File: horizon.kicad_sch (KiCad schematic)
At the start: 102 parts, among them IC1 A3909, J1 Micro_SD_Card_Det1, J10 Conn_01x02_Pin, J2 Conn_02x03_Counter_Clockwise, J7 Conn_02x03_Counter_Clockwise, J8 Conn_02x03_Counter_Clockwise, J9 USB_C_Receptacle_USB2.0_16P, Q2 DMG2301L, SW1 SW_Rotary_1x3_MP, SW2 SW_Rotary_1x3_MP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

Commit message: INTCOMM Completed
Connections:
- net scl: no longer U3.43 (PA22), U4.43 (PA22)
- net sda: no longer U3.44 (PA23), U4.44 (PA23)
- net PTA12: now reaches U1.29 (D4/CAN-RX/PWM)
- net I2C0_SCL: now reaches U1.37 (D19/A5/SCL0/TOUCH)
- net I2C0_SCL: now also U3.44 (PA23), U4.44 (PA23)
- net I2C0_SDA: now reaches U1.38 (D18/A4/SDA0/TOUCH)
- net I2C0_SDA: now also U3.43 (PA22), U4.43 (PA22)
- net PTD4: now reaches U1.57 (D2)
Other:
- note added: "INT from NAV"
- note added: "INT from TLM"
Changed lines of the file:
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@@
 		)
 	)
+	(text "INT from TLM"
+		(exclude_from_sim no)
+		(at 307.086 140.208 0)
+		(effects
+			(font
+				(size 1.27 1.27)
+			)
+		)
+	)
 	(text "GPS → MCU RX"
 		(exclude_from_sim no)
@@
 		)
 	)
-	(text "For NAND and SD"
+	(text "INT from NAV"
 		(exclude_from_sim no)
-		(at 293.37 160.274 0)
+		(at 307.848 135.128 0)
 		(effects
 			(font
@@
 		)
 	)
+	(global_label "PTD4"
+		(shape input)
+		(at 322.58 134.62 180)
+		(fields_autoplaced yes)
+		(effects
+			(font
+				(size 1.27 1.27)
+			)
+			(justify right)
+		)
+		(property "Intersheetrefs" "${INTERSHEET_REFS}"
+			(at 314.8777 134.62 0)
+			(effects
+				(font
+					(size 1.27 1.27)
+				)
+				(justify right)
+				(hide yes)
+			)
+		)
+	)
 	(global_label "SWCLK MMCU"
 		(shape input)
@@
 		)
 	)
-	(global_label "scl"
+	(global_label "I2C0_SDA"
 		(shape input)
 		(at 113.03 198.12 180)
@@
 		)
 		(property "Intersheetrefs" "${INTERSHEET_REFS}"
-			(at 107.2629 198.12 0)
+			(at 101.2153 198.12 0)
 			(effects
 				(font
@@
 		)
 	)
-	(global_label "sda"
+	(global_label "I2C0_SCL"
 		(shape input)
 		(at 113.03 200.66 180)
@@
 		)
 		(property "Intersheetrefs" "${INTERSHEET_REFS}"
-			(at 106.7187 200.66 0)
+			(at 101.2758 200.66 0)
 			(effects
 				(font
@@
 		)
 	)
+	(global_label "I2C0_SCL"
+		(shape input)
+		(at 322.58 177.8 180)
+		(fields_autoplaced yes)
+		(effects
+			(font
+				(size 1.27 1.27)
+			)
+			(justify right)
+		)
+		(property "Intersheetrefs" "${INTERSHEET_REFS}"
+			(at 310.8258 177.8 0)
+			(effects
+				(font
+					(size 1.27 1.27)
+				)
+				(justify right)
+				(hide yes)
+			)
+		)
+	)
 	(global_label "SPI_CLOCK TMCU"
 		(shape input)
@@
 		)
 	)
+	(global_label "PTA12"
+		(shape input)
+		(at 322.58 139.7 180)
+		(fields_autoplaced yes)
+		(effects
+			(font
+				(size 1.27 1.27)
+			)
+			(justify right)
+		)
+		(property "Intersheetrefs" "${INTERSHEET_REFS}"
+			(at 313.8496 139.7 0)
+			(effects
+				(font
+					(size 1.27 1.27)
+				)
+				(justify right)
+				(hide yes)
+			)
+		)
+	)
 	(global_label " SPI0_SCK MMCU"
 		(shape input)
@@
 		)
 	)
-	(global_label "scl"
+	(global_label "I2C0_SDA"
 		(shape input)
 		(at 17.78 194.31 180)
@@
 		)
 		(property "Intersheetrefs" "${INTERSHEET_REFS}"
-			(at 12.0129 194.31 0)
+			(at 5.9653 194.31 0)
 			(effects
 				(font
@@
 		)
 	)
+	(global_label "I2C0_SDA"
+		(shape input)
+		(at 322.58 175.26 180)
+		(fields_autoplaced yes)
+		(effects
+			(font
+				(size 1.27 1.27)
+			)
+			(justify right)
+		)
+		(property "Intersheetrefs" "${INTERSHEET_REFS}"
+			(at 310.7653 175.26 0)
+			(effects
+				(font
+					(size 1.27 1.27)
+				)
+				(justify right)
+				(hide yes)
+			)
+		)
+	)
 	(global_label "bat"
 		(shape input)
@@
 		)
 	)
-	(global_label "sda"
+	(global_label "I2C0_SCL"
 		(shape input)
 		(at 17.78 196.85 180)
@@
 		)
 		(property "Intersheetrefs" "${INTERSHEET_REFS}"
-			(at 11.4687 196.85 0)
+			(at 6.0258 196.85 0)
 			(effects
 				(font

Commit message: Labels
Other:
- note added: "SERCOM Stuff For Firmware INTCOMM"
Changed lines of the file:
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@@
 	(generator_version "9.0")
 	(paper "A4")
+	(text "SERCOM Stuff For Firmware INTCOMM"
+		(exclude_from_sim no)
+		(at 292.608 176.784 0)
+		(effects
+			(font
+				(size 1.27 1.27)
+			)
+		)
+	)
 	(text "For NAND and SD"
 		(exclude_from_sim no)
@@
 		)
 	)
+	(text "SERCOM Stuff For Firmware INTCOMM"
+		(exclude_from_sim no)
+		(at 83.058 199.898 0)
+		(effects
+			(font
+				(size 1.27 1.27)
+			)
+		)
+	)
 	(text "MCU → GPS TX"
 		(exclude_from_sim no)
@@
 		(effects
 			(font
+				(size 1.27 1.27)
+			)
+		)
+	)
+	(text "SERCOM Stuff For Firmware INTCOMM"
+		(exclude_from_sim no)
+		(at -13.462 195.58 0)
+		(effects
+			(font

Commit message: set up hierarchy
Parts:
- removed C10: 4n7, Capacitor_SMD:C_0603_1608Metric, symbol Device:C
- removed C14: 0.1µF, symbol Device:C
- removed C15: 0.1 µF, symbol Device:C
- removed C26: 100n, Capacitor_SMD:C_0603_1608Metric, symbol Device:C
- removed C28, C32, C40, C41, C42, C43: 10uF, Capacitor_SMD:C_0603_1608Metric, symbol Device:C
- removed C29, C37: 10u, Capacitor_SMD:C_0603_1608Metric, symbol Device:C
- removed C30, C38: 2u2, Capacitor_SMD:C_0603_1608Metric, symbol Device:C
- removed C31, C39: 100u, Capacitor_THT:CP_Radial_D4.0mm_P2.00mm, symbol Device:C_Polarized_US
- removed C33: 3.3 nF, Capacitor_SMD:C_0603_1608Metric, symbol Device:C
- removed C34: 22uF, Capacitor_SMD:C_0603_1608Metric, symbol Device:C
- removed C35: 1uF, Capacitor_SMD:C_0603_1608Metric, symbol Device:C
- removed C36: 1u, Capacitor_SMD:C_0603_1608Metric, symbol Device:C
- removed D19, D20, D23, D24, D25: PMEG6020ER, Diode_SMD:Nexperia_CFP3_SOD-123W, symbol Diode:PMEG6020ER
- removed D21, D22, D5: LED, LED_SMD:LED_0201_0603Metric, symbol Device:LED
- removed D6: PRTR5V0U2X, Package_TO_SOT_SMD:SOT-143, symbol Power_Protection:PRTR5V0U2X
- removed FL3, FL4: Choke_CommonMode_PulseElectronics_PH9455x105NL, Inductor_THT:L_CommonMode_PulseElectronics_PH9455x105NL_1, symbol Filter:Choke_CommonMode_PulseElectronics_PH9455x105NL
- removed IC1: A3909, A3909:MSOP10-PAD, symbol A3909:A3909
- removed J1: Micro_SD_Card_Det1, symbol Connector:Micro_SD_Card_Det1
- removed J10: Conn_01x02_Pin, Connector_JST:JST_PH_B2B-PH-K_1x02_P2.00mm_Vertical, symbol Connector:Conn_01x02_Pin
- removed J9: USB_C_Receptacle_USB2.0_16P, Connector_USB:USB_C_Receptacle_Amphenol_124019772112A, symbol Connector:USB_C_Receptacle_USB2.0_16P
- removed L2, L3, L4: SLF7055T-6R8N2R8-3PF, Inductor_SMD:L_7.3x7.3_H4.5, symbol SLF7055T-6R8N2R8-3PF[1]:SLF7055T-6R8N2R8-3PF
- removed Q2: DMG2301L, Package_TO_SOT_SMD:SOT-23, symbol Transistor_FET:DMG2301L
- removed R1: 90k, symbol Device:R
- removed R10, R11, R12, R13, R8, R9: 10kΩ, symbol Device:R
- removed R17, R18: 5k1, Resistor_SMD:R_0603_1608Metric, symbol Device:R
- removed R19, R47: 330, Resistor_SMD:R_0603_1608Metric, symbol Device:R
- removed R2: 10k, symbol Device:R
- removed R40, R41, R43, R45, R48, R49, R51: 100k, Resistor_SMD:R_0603_1608Metric, symbol Device:R
- removed R42, R50: 315k, Resistor_SMD:R_0603_1608Metric, symbol Device:R
- removed R44: 350k, Resistor_SMD:R_0603_1608Metric, symbol Device:R
- removed R46: 100, Resistor_SMD:R_0603_1608Metric, symbol Device:R
- removed SW1, SW2: SW_Rotary_1x3_MP, symbol Switch:SW_Rotary_1x3_MP
- removed TP10, TP11: TestPoint, TestPoint:TestPoint_Pad_1.0x1.0mm, symbol Connector:TestPoint
- removed U12: TPS63061, Package_SON:Texas_S-PWSON-N10_ThermalVias, symbol Regulator_Switching:TPS63061
- removed U13: LTC4412xS6, Package_TO_SOT_SMD:TSOT-23-6, symbol Power_Management:LTC4412xS6
- removed U14, U16: TPS61092, Package_DFN_QFN:Texas_RSA_VQFN-16-1EP_4x4mm_P0.65mm_EP2.7x2.7mm_ThermalVias, symbol Regulator_Switching:TPS61092
- removed U15: AP2112K-3.3, Package_TO_SOT_SMD:SOT-23-5, symbol Regulator_Linear:AP2112K-3.3
- removed U2: IMU, BNO086:IC_BNO086, symbol BNO086:BNO086
- removed U5: LPS22HB, Package_LGA:ST_HLGA-10_2x2mm_P0.5mm_LayoutBorder3x2y, symbol Sensor_Pressure:LPS22HB
- removed U6: GPS, L96-M33:XCVR_L96-M33, symbol L96-M33:L96-M33
- removed U7: SX1276, Package_DFN_QFN:QFN-28-1EP_6x6mm_P0.65mm_EP4.8x4.8mm, symbol RF:SX1276
- removed U8: NAND, Package_SO:SOIC-8_5.3x5.3mm_P1.27mm, symbol Memory_Flash:W25Q128JVS
- removed U9: TPS82130, Package_LGA:Texas_SIL0008D_MicroSiP-8-1EP_2.8x3mm_P0.65mm_EP1.1x1.9mm_ThermalVias, symbol Regulator_Switching:TPS82130
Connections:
- no-connect marks 12 -> 3
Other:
- added sheet input usb (usb.kicad_sch)
- added sheet power stuff (power.kicad_sch)
- added sheet sensors (sensor.kicad_sch)
- note removed: "CHANGE TO GPIO PINS FOR SOFTWARE RESET"
- note removed: "TIE IT TO LOW to internal occilator"
- moved on the sheet: C1, C11, C12, C13, C2, C3, C4, C5, C6, C7, C8, C9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

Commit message: Changes, idr what though :(
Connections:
- net +3.3V: now also U1.21 (VBAT)
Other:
- note added: "IIC Bus lines for Sensors (not including NAND, SD-CARD)"
- note added: "USB Data Lines for Programming"
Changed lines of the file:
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@@
 	(generator_version "9.0")
 	(paper "A4")
-	(text "SERCOM Stuff For Firmware INTCOMM"
+	(text "SERCOM Stuff For Firmware \nINTCOMM"
 		(exclude_from_sim no)
-		(at 192.278 101.854 0)
+		(at 197.104 101.854 0)
 		(effects
 			(font
@@
 	(text "For NAND and SD"
 		(exclude_from_sim no)
-		(at 193.548 82.55 0)
+		(at 193.802 84.074 0)
 		(effects
 			(font
@@
 		)
 	)
-	(text "SERCOM Stuff For Firmware INTCOMM"
+	(text "SERCOM Stuff For Firmware \nINTCOMM"
 		(exclude_from_sim no)
-		(at 98.298 124.968 0)
+		(at 103.124 124.714 0)
 		(effects
 			(font
@@
 		)
 	)
+	(text "USB Data Lines for \nProgramming"
+		(exclude_from_sim no)
+		(at 104.14 129.794 0)
+		(effects
+			(font
+				(size 1.27 1.27)
+			)
+		)
+	)
+	(text "IIC Bus lines for Sensors \n(not including NAND, SD-CARD)"
+		(exclude_from_sim no)
+		(at 99.314 94.234 0)
+		(effects
+			(font
+				(size 1.27 1.27)
+			)
+		)
+	)
 	(junction
 		(at 148.59 52.07)
@@
 	)
 	(symbol
+		(lib_id "power:+3.3V")
+		(at 280.67 105.41 270)
+		(unit 1)
+		(exclude_from_sim no)
+		(in_bom yes)
+		(on_board yes)
+		(dnp no)
+		(fields_autoplaced yes)
+		(property "Reference" "#PWR030"
+			(at 276.86 105.41 0)
+			(effects
+				(font
+					(size 1.27 1.27)
+				)
+				(hide yes)
+			)
+		)
+		(property "Value" "+3.3V"
+			(at 284.48 105.4099 90)
+			(effects
+				(font
+					(size 1.27 1.27)
+				)
+				(justify left)
+			)
+		)
+		(property "Footprint" ""
+			(at 280.67 105.41 0)
+			(effects
+				(font
+					(size 1.27 1.27)
+				)
+				(hide yes)
+			)
+		)
+		(property "Datasheet" ""
+			(at 280.67 105.41 0)
+			(effects
+				(font
+					(size 1.27 1.27)
+				)
+				(hide yes)
+			)
+		)
+		(property "Description" "Power symbol creates a global label with name \"+3.3V\""
+			(at 280.67 105.41 0)
+			(effects
+				(font
+					(size 1.27 1.27)
+				)
+				(hide yes)
+			)
+		)
+		(pin "1"
+		)
+		(instances
+			(project ""
+				(path "/78d9c2f3-deae-418a-8c21-4820ea8fc57f"
+					(reference "#PWR030")
+					(unit 1)
+				)
+			)
+		)
+	)
+	(symbol
 		(lib_id "Connector_Generic:Conn_02x03_Counter_Clockwise")
 		(at 41.91 168.91 0)
@@
 		)
 		(property "Value" "+3.3V"
-			(at 179.07 118.11 0)
+			(at 194.056 117.856 0)
 			(effects
 				(font
@@
 		)
 		(property "Value" "+3.3V"
-			(at 185.42 115.57 0)
+			(at 200.66 116.586 0)
 			(effects
 				(font

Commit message: misc fixes
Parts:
- added C10, C17: 12pF, symbol Device:C
- added Y1: Crystal, symbol Device:Crystal
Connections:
- net GND: now also C10.2, C17.2
- net at U1.19 (XTAL32): now also C10.1, Y1.2
- net at U1.20 (EXTAL32): now also C17.1, Y1.1

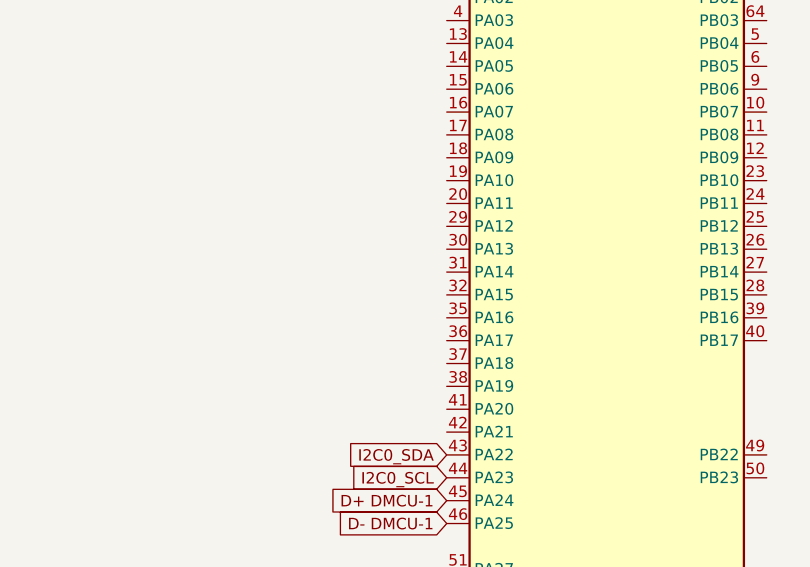
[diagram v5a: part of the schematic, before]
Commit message: H-Bridge is done!
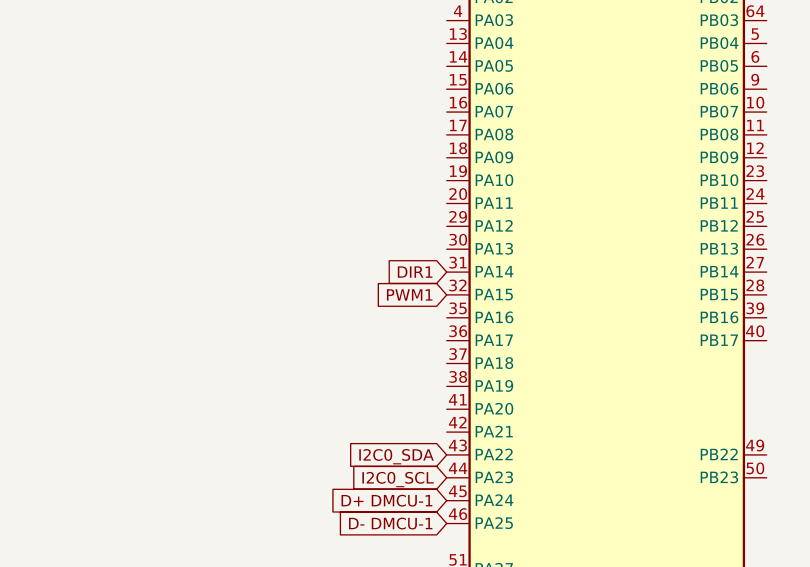
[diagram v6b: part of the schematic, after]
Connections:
- net DIR1: now reaches U3.31 (PA14)
- net PWM1: now reaches U3.32 (PA15)
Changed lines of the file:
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@@
+		)
+	)
+	(global_label "DIR1"
+		(shape input)
+		(at 33.02 99.06 180)
+		(fields_autoplaced yes)
+		(effects
+			(font
+				(size 1.27 1.27)
+			)
+			(justify right)
+		)
+		(property "Intersheetrefs" "${INTERSHEET_REFS}"
+			(at 25.6805 99.06 0)
+			(effects
+				(font
+					(size 1.27 1.27)
+				)
+				(justify right)
+				(hide yes)
+			)
 		)
 	)
@@
 			(effects
 				(font
+					(size 1.27 1.27)
+				)
+				(justify right)
+				(hide yes)
+			)
+		)
+	)
+	(global_label "PWM1"
+		(shape input)
+		(at 33.02 101.6 180)
+		(fields_autoplaced yes)
+		(effects
+			(font
+				(size 1.27 1.27)
+			)
+			(justify right)
+		)
+		(property "Intersheetrefs" "${INTERSHEET_REFS}"
+			(at 24.6525 101.6 0)
+			(effects
+				(font

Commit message: Changes
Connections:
- net Baro_int TMCU: now reaches U4.17 (PA08)
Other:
- note added: "Outputs a signal when data is ready"
- note added: "SPI Bus lines for Sensors (not including NAND, SD-CARD)"
- note removed: "IIC Bus lines for Sensors (not including NAND, SD-CARD)"
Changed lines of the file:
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@@
+		)
+	)
+	(text "Outputs a signal when data is ready"
+		(exclude_from_sim no)
+		(at 93.472 87.376 0)
+		(effects
+			(font
+				(size 1.27 1.27)
+			)
 		)
 	)
@@
 		)
 	)
-	(text "IIC Bus lines for Sensors \n(not including NAND, SD-CARD)"
+	(text "SPI Bus lines for Sensors \n(not including NAND, SD-CARD)"
 		(exclude_from_sim no)
 		(at 99.314 94.234 0)
@@
 			(effects
 				(font
+					(size 1.27 1.27)
+				)
+				(justify right)
+				(hide yes)
+			)
+		)
+	)
+	(global_label "Baro_int TMCU"
+		(shape input)
+		(at 128.27 87.63 180)
+		(fields_autoplaced yes)
+		(effects
+			(font
+				(size 1.27 1.27)
+			)
+			(justify right)
+		)
+		(property "Intersheetrefs" "${INTERSHEET_REFS}"
+			(at 111.4964 87.63 0)
+			(effects
+				(font

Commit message: Flag Changes- Important
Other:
- note added: "Clock pin For NAND and SD"
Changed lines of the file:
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@@
 		)
 	)
-	(text "For NAND and SD"
+	(text "Clock pin For NAND and SD"
 		(exclude_from_sim no)
 		(at 211.582 122.682 0)
